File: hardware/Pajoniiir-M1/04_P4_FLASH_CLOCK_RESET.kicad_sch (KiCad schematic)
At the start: 21 parts, among them U2 W25Q128JVPIQ, Y1 ECS-400-10-37B2-CKY-TR

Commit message: hardware: realign crystal ground pins to KiCad 9 symbol
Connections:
- net GND: no longer Y1.2 (G), Y1.4 (G)
- new net: Y1.2 (G), Y1.4 (G)
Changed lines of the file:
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@@
   (hierarchical_label "XTAL_N" (shape bidirectional) (at 193.675 64.77 0) (effects (font (size 1.27 1.27))))
   (symbol
-    (lib_id "power:GND") (at 189.865 69.85 0) (unit 1)
+    (lib_id "power:GND") (at 189.865 68.58 0) (unit 1)
     (exclude_from_sim no) (in_bom yes) (on_board yes) (dnp no)
-    (property "Reference" "#PWR0403" (at 189.865 75.85 0) (effects (font (size 1.27 1.27)) (hide yes)))
-    (property "Value" "GND" (at 189.865 72.85 0) (effects (font (size 1.27 1.27))))
-    (property "Footprint" "" (at 189.865 69.85 0) (effects (font (size 1.27 1.27)) (hide yes)))
-    (property "Datasheet" "" (at 189.865 69.85 0) (effects (font (size 1.27 1.27)) (hide yes)))
+    (property "Reference" "#PWR0403" (at 189.865 74.58 0) (effects (font (size 1.27 1.27)) (hide yes)))
+    (property "Value" "GND" (at 189.865 71.58 0) (effects (font (size 1.27 1.27))))
+    (property "Footprint" "" (at 189.865 68.58 0) (effects (font (size 1.27 1.27)) (hide yes)))
+    (property "Datasheet" "" (at 189.865 68.58 0) (effects (font (size 1.27 1.27)) (hide yes)))
     (pin "1")
     (instances (project "Pajoniiir-M1" (path "/2c8dd352-b7b8-4d9e-8f93-5dd43be2a100/31000004-6b2a-4a3a-8c91-000000000004" (reference "#PWR0403") (unit 1))))
   )
   (symbol
-    (lib_id "power:GND") (at 189.865 59.69 0) (unit 1)
+    (lib_id "power:GND") (at 189.865 60.96 0) (unit 1)
     (exclude_from_sim no) (in_bom yes) (on_board yes) (dnp no)
-    (property "Reference" "#PWR0404" (at 189.865 65.69 0) (effects (font (size 1.27 1.27)) (hide yes)))
-    (property "Value" "GND" (at 189.865 62.69 0) (effects (font (size 1.27 1.27))))
-    (property "Footprint" "" (at 189.865 59.69 0) (effects (font (size 1.27 1.27)) (hide yes)))
-    (property "Datasheet" "" (at 189.865 59.69 0) (effects (font (size 1.27 1.27)) (hide yes)))
+    (property "Reference" "#PWR0404" (at 189.865 66.96 0) (effects (font (size 1.27 1.27)) (hide yes)))
+    (property "Value" "GND" (at 189.865 63.96 0) (effects (font (size 1.27 1.27))))
+    (property "Footprint" "" (at 189.865 60.96 0) (effects (font (size 1.27 1.27)) (hide yes)))
+    (property "Datasheet" "" (at 189.865 60.96 0) (effects (font (size 1.27 1.27)) (hide yes)))
     (pin "1")
     (instances (project "Pajoniiir-M1" (path "/2c8dd352-b7b8-4d9e-8f93-5dd43be2a100/31000004-6b2a-4a3a-8c91-000000000004" (reference "#PWR0404") (unit 1))))

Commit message: hardware: stabilize system buck and crystal symbols
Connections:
- net GND: now also Y1.2 (G), Y1.4 (G)
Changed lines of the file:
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@@
   (hierarchical_label "XTAL_N" (shape bidirectional) (at 193.675 64.77 0) (effects (font (size 1.27 1.27))))
   (symbol
-    (lib_id "power:GND") (at 189.865 68.58 0) (unit 1)
+    (lib_id "power:GND") (at 189.865 69.85 0) (unit 1)
     (exclude_from_sim no) (in_bom yes) (on_board yes) (dnp no)
-    (property "Reference" "#PWR0403" (at 189.865 74.58 0) (effects (font (size 1.27 1.27)) (hide yes)))
-    (property "Value" "GND" (at 189.865 71.58 0) (effects (font (size 1.27 1.27))))
-    (property "Footprint" "" (at 189.865 68.58 0) (effects (font (size 1.27 1.27)) (hide yes)))
-    (property "Datasheet" "" (at 189.865 68.58 0) (effects (font (size 1.27 1.27)) (hide yes)))
+    (property "Reference" "#PWR0403" (at 189.865 75.85 0) (effects (font (size 1.27 1.27)) (hide yes)))
+    (property "Value" "GND" (at 189.865 72.85 0) (effects (font (size 1.27 1.27))))
+    (property "Footprint" "" (at 189.865 69.85 0) (effects (font (size 1.27 1.27)) (hide yes)))
+    (property "Datasheet" "" (at 189.865 69.85 0) (effects (font (size 1.27 1.27)) (hide yes)))
     (pin "1")
     (instances (project "Pajoniiir-M1" (path "/2c8dd352-b7b8-4d9e-8f93-5dd43be2a100/31000004-6b2a-4a3a-8c91-000000000004" (reference "#PWR0403") (unit 1))))
   )
   (symbol
-    (lib_id "power:GND") (at 189.865 60.96 0) (unit 1)
-    (exclude_from_sim no) (in_bom yes) (on_board yes) (dnp no)
-    (property "Reference" "#PWR0404" (at 189.865 66.96 0) (effects (font (size 1.27 1.27)) (hide yes)))
-    (property "Value" "GND" (at 189.865 63.96 0) (effects (font (size 1.27 1.27))))
-    (property "Footprint" "" (at 189.865 60.96 0) (effects (font (size 1.27 1.27)) (hide yes)))
-    (property "Datasheet" "" (at 189.865 60.96 0) (effects (font (size 1.27 1.27)) (hide yes)))
-    (pin "1")
-    (instances (project "Pajoniiir-M1" (path "/2c8dd352-b7b8-4d9e-8f93-5dd43be2a100/31000004-6b2a-4a3a-8c91-000000000004" (reference "#PWR0404") (unit 1))))
-  )
-  (symbol

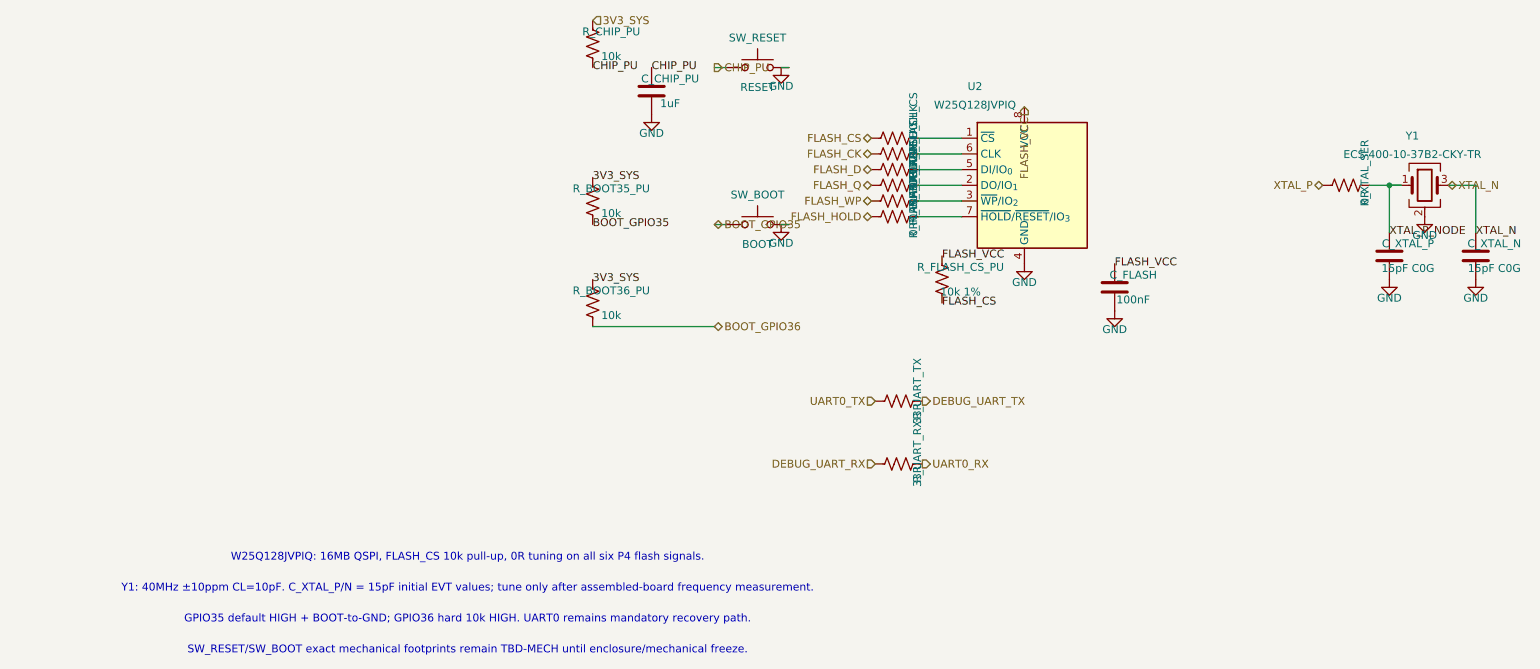
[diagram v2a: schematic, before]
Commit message: hardware: normalize schematic reference designators
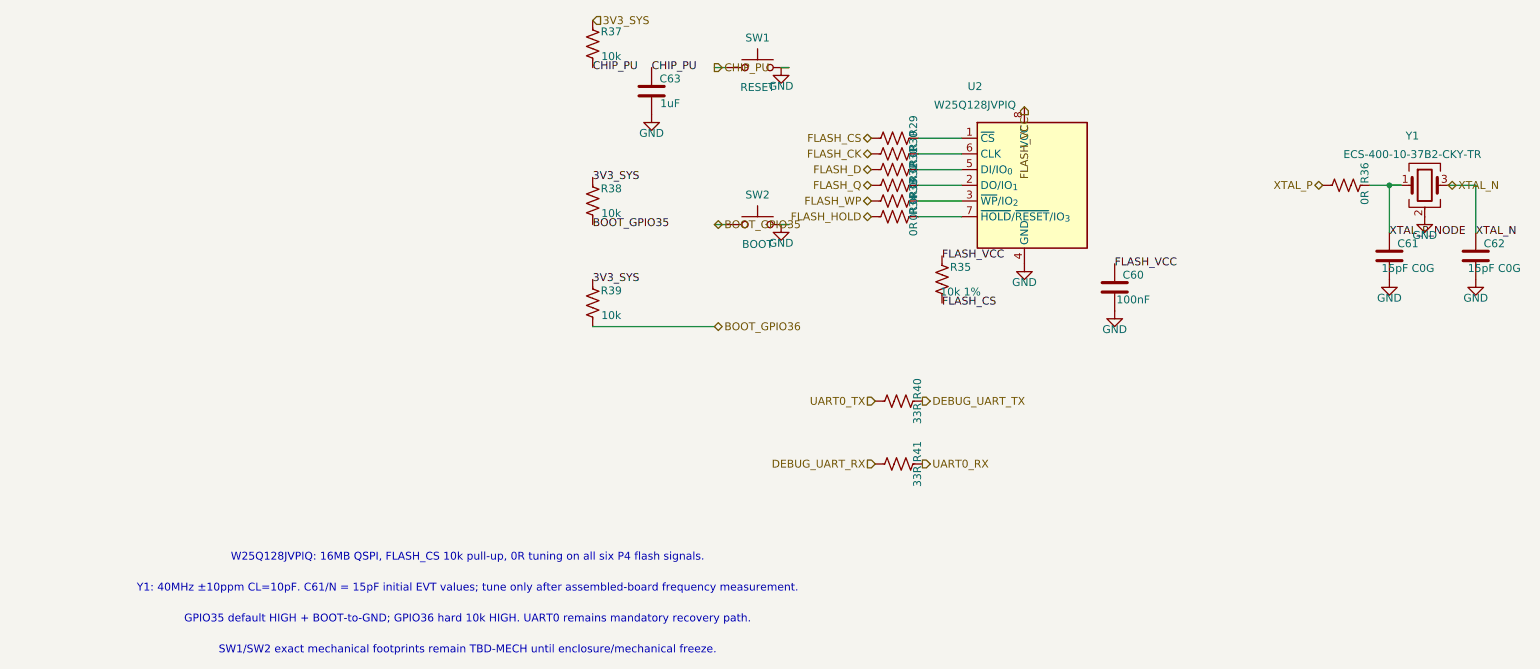
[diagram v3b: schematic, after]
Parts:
- renumbered C_FLASH to C60, C_XTAL_P to C61, C_XTAL_N to C62, C_CHIP_PU to C63, R_FLASH_CS to R29, R_FLASH_CLK to R30, R_FLASH_D0 to R31, R_FLASH_D1 to R32, R_FLASH_D2 to R33, R_FLASH_D3 to R34, R_FLASH_CS_PU to R35, R_XTAL_SER to R36, R_CHIP_PU to R37, R_BOOT35_PU to R38, R_BOOT36_PU to R39, R_UART_TX to R40, R_UART_RX to R41, SW_RESET to SW1, SW_BOOT to SW2
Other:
- note added: "SW1/SW2 exact mechanical footprints remain TBD-MECH until enclosure/mechanical freeze."
- note added: "Y1: 40MHz ±10ppm CL=10pF. C61/N = 15pF initial EVT values; tune only after assembled-board frequency measurement."
- note removed: "SW_RESET/SW_BOOT exact mechanical footprints remain TBD-MECH until enclosure/mechanical freeze."
- note removed: "Y1: 40MHz ±10ppm CL=10pF. C_XTAL_P/N = 15pF initial EVT values; tune only after assembled-board frequency measurement."

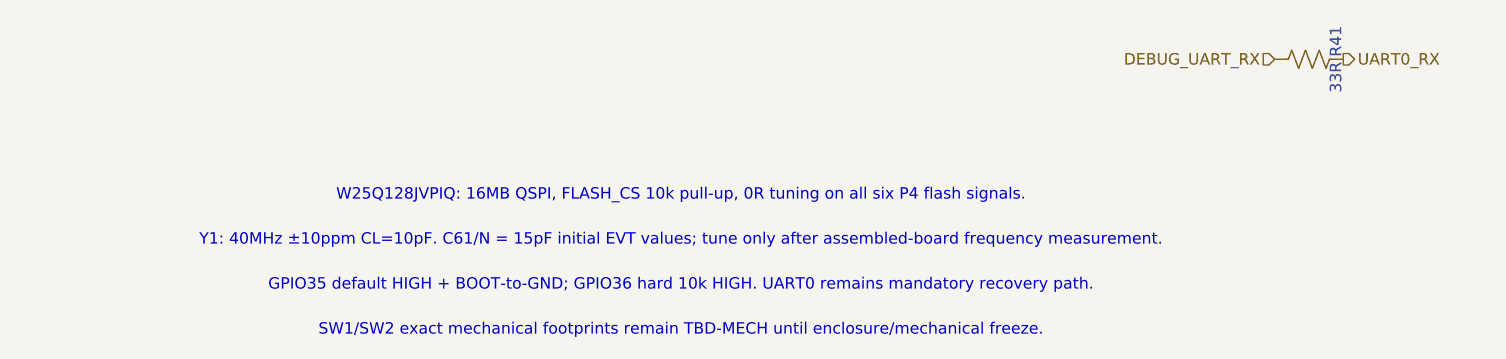
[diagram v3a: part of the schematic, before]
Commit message: hardware: constrain RefDes migration to annotation fields
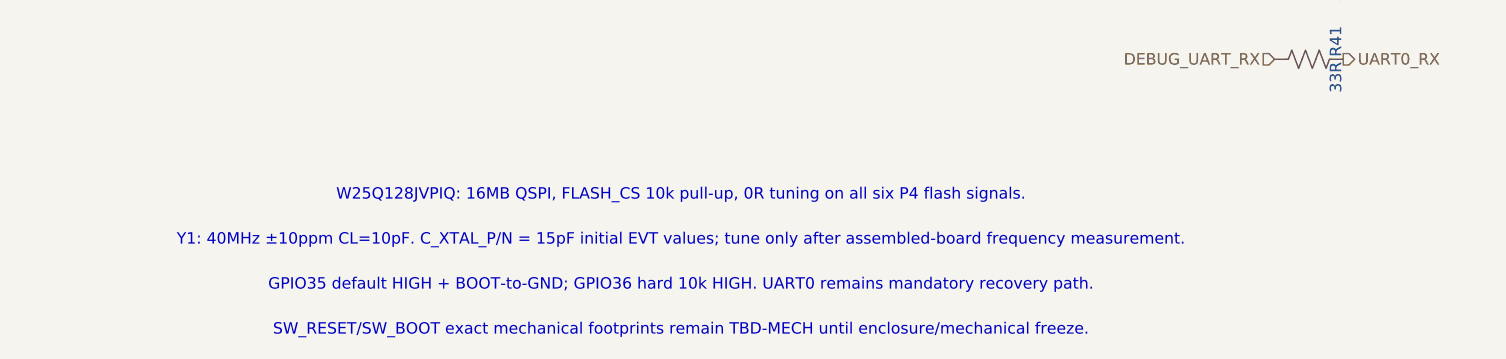
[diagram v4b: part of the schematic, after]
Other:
- note added: "SW_RESET/SW_BOOT exact mechanical footprints remain TBD-MECH until enclosure/mechanical freeze."
- note added: "Y1: 40MHz ±10ppm CL=10pF. C_XTAL_P/N = 15pF initial EVT values; tune only after assembled-board frequency measurement."
- note removed: "SW1/SW2 exact mechanical footprints remain TBD-MECH until enclosure/mechanical freeze."
- note removed: "Y1: 40MHz ±10ppm CL=10pF. C61/N = 15pF initial EVT values; tune only after assembled-board frequency measurement."
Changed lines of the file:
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@@
   (hierarchical_label "UART0_RX" (shape output) (at 108.585 109.855 0) (effects (font (size 1.27 1.27))))
   (text "W25Q128JVPIQ: 16MB QSPI, FLASH_CS 10k pull-up, 0R tuning on all six P4 flash signals." (exclude_from_sim no) (at 35 125 0) (effects (font (size 1.27 1.27))))
-  (text "Y1: 40MHz ±10ppm CL=10pF. C61/N = 15pF initial EVT values; tune only after assembled-board frequency measurement." (exclude_from_sim no) (at 35 130 0) (effects (font (size 1.27 1.27))))
+  (text "Y1: 40MHz ±10ppm CL=10pF. C_XTAL_P/N = 15pF initial EVT values; tune only after assembled-board frequency measurement." (exclude_from_sim no) (at 35 130 0) (effects (font (size 1.27 1.27))))
   (text "GPIO35 default HIGH + BOOT-to-GND; GPIO36 hard 10k HIGH. UART0 remains mandatory recovery path." (exclude_from_sim no) (at 35 135 0) (effects (font (size 1.27 1.27))))
-  (text "SW1/SW2 exact mechanical footprints remain TBD-MECH until enclosure/mechanical freeze." (exclude_from_sim no) (at 35 140 0) (effects (font (size 1.27 1.27))))
+  (text "SW_RESET/SW_BOOT exact mechanical footprints remain TBD-MECH until enclosure/mechanical freeze." (exclude_from_sim no) (at 35 140 0) (effects (font (size 1.27 1.27))))
   (sheet_instances (path "/" (page "5")))
   (embedded_fonts no)
